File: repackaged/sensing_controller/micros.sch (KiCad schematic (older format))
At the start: 6 parts

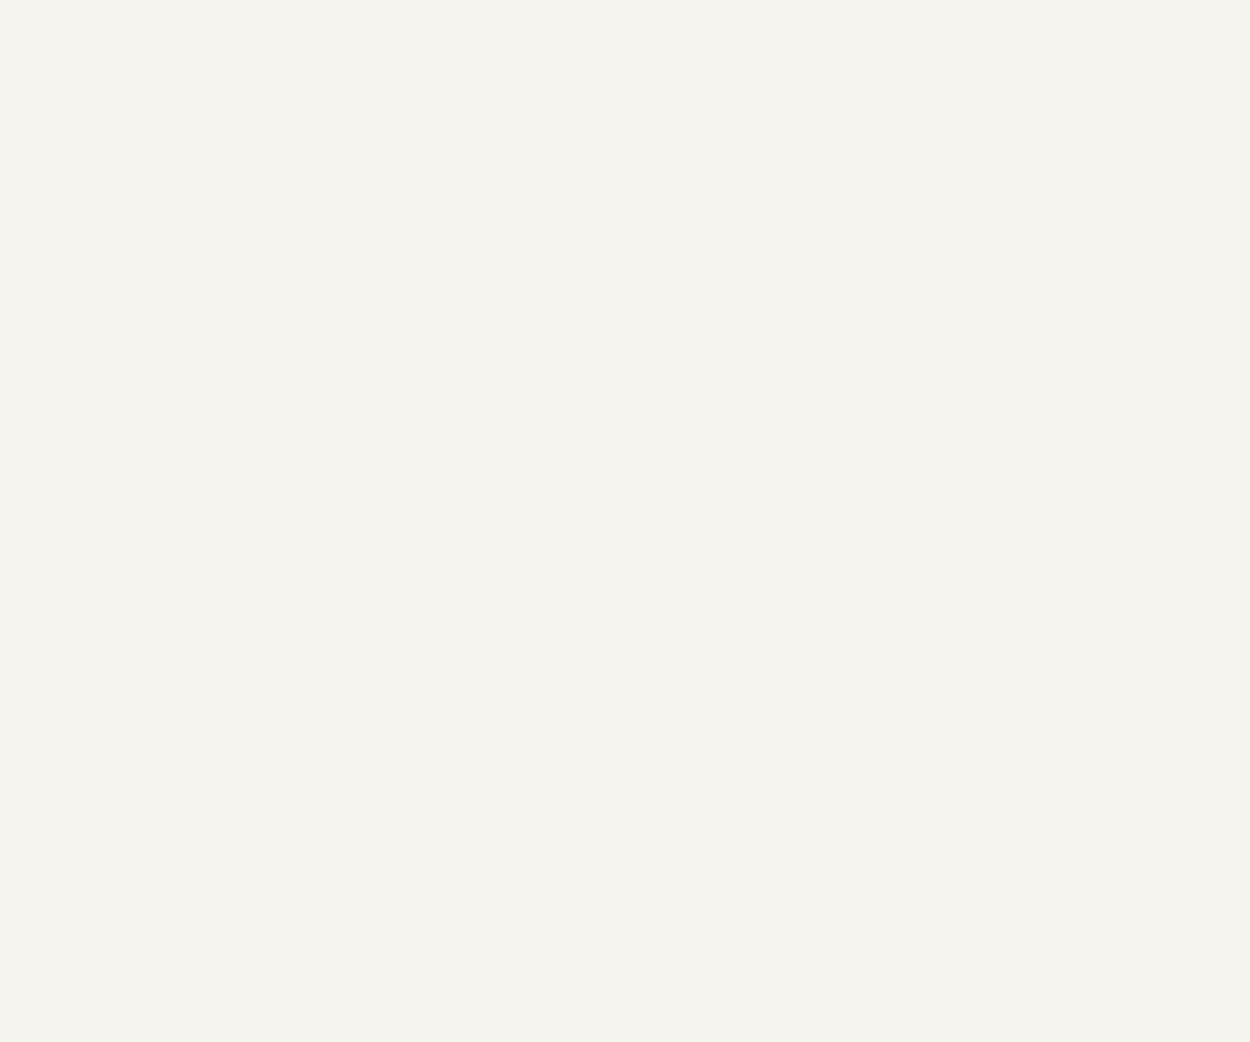
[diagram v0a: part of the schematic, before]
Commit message: Add micro.sch with added components.
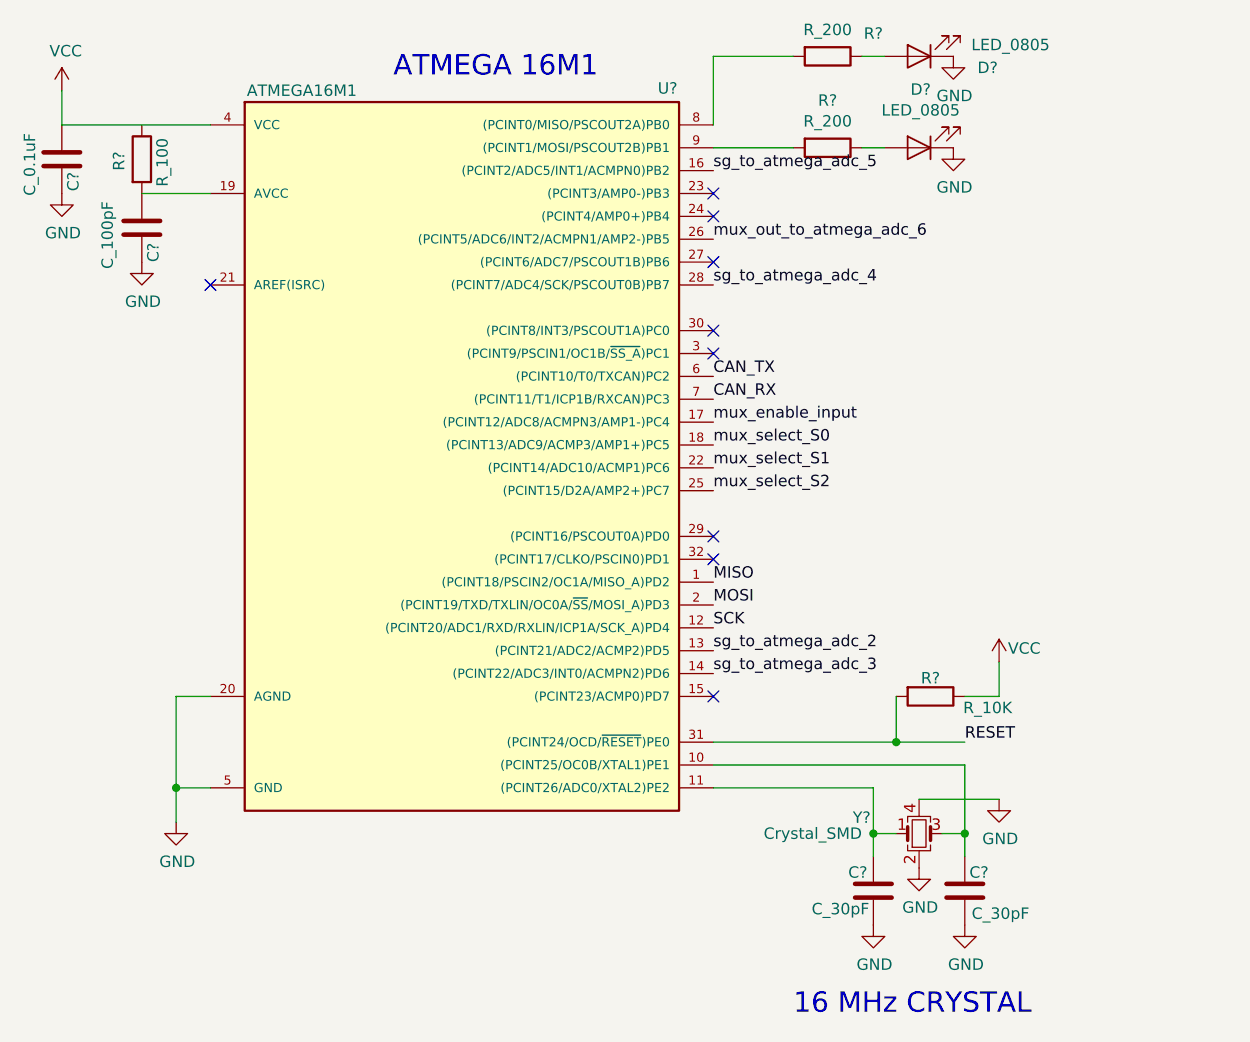
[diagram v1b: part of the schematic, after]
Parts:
- added C?: C_100pF, footprints:C_0805_OEM, symbol formula:C_100pF
- added C? (x2): C_30pF, footprints:C_0805_OEM, symbol formula:C_30pF
- added C?: C_0.1uF, footprints:C_0805_OEM, symbol formula:C_0.1uF
- added D? (x2): LED_0805, footprints:LED_0805_OEM, symbol formula:LED_0805
- added R?: R_100, footprints:R_0805_OEM, symbol formula:R_100
- added R?: R_10K, footprints:R_0805_OEM, symbol formula:R_10K
- added R? (x2): R_200, footprints:R_0805_OEM, symbol formula:R_200
- added U?: ATMEGA16M1, footprints:TQFP-32_7x7mm_Pitch0.8mm, symbol formula:ATMEGA16M1
- added Y?: Crystal_SMD, footprints:Crystal_SMD_FA238, symbol formula:Crystal_SMD
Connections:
- net GND: now also C?.2, C?.2, C?.2, C?.2, D?.1 (K), D?.1 (K), U?.20 (AGND), U?.5 (GND), Y?.2, Y?.4
- new net: C?.1, R?.2, U?.19 (AVCC)
- new net: C?.1, U?.11 ((PCINT26/ADC0/XTAL2)PE2), Y?.1
- new net: C?.1, U?.10 ((PCINT25/OC0B/XTAL1)PE1), Y?.3
- new net: R?.2, U?.8 ((PCINT0/MISO/PSCOUT2A)PB0)
- new net: R?.2, U?.9 ((PCINT1/MOSI/PSCOUT2B)PB1)
- new net: D?.2 (A), R?.1 (x2)
- new net CAN_RX: U?.7 ((PCINT11/T1/ICP1B/RXCAN)PC3)
- new net CAN_TX: U?.6 ((PCINT10/T0/TXCAN)PC2)
- new net MISO: U?.1 ((PCINT18/PSCIN2/OC1A/MISO_A)PD2)
- new net MOSI: U?.2 ((PCINT19/TXD/TXLIN/OC0A/~SS~/MOSI_A)PD3)
- new net RESET: R?.2, U?.31 ((PCINT24/OCD/~RESET~)PE0)
- new net SCK: U?.12 ((PCINT20/ADC1/RXD/RXLIN/ICP1A/SCK_A)PD4)
- new net VCC: C?.1, R?.1, U?.4 (VCC)
- new net mux_enable_input: U?.17 ((PCINT12/ADC8/ACMPN3/AMP1-)PC4)
- new net mux_out_to_atmega_adc_6: U?.26 ((PCINT5/ADC6/INT2/ACMPN1/AMP2-)PB5)
- new net mux_select_S0: U?.18 ((PCINT13/ADC9/ACMP3/AMP1+)PC5)
- new net mux_select_S1: U?.22 ((PCINT14/ADC10/ACMP1)PC6)
- new net mux_select_S2: U?.25 ((PCINT15/D2A/AMP2+)PC7)
- new net sg_to_atmega_adc_2: U?.13 ((PCINT21/ADC2/ACMP2)PD5)
- new net sg_to_atmega_adc_3: U?.14 ((PCINT22/ADC3/INT0/ACMPN2)PD6)
- new net sg_to_atmega_adc_4: U?.28 ((PCINT7/ADC4/SCK/PSCOUT0B)PB7)
- new net sg_to_atmega_adc_5: U?.16 ((PCINT2/ADC5/INT1/ACMPN0)PB2)
- no-connect marks 15 -> 24
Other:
- note added: "ATMEGA 16M1\n"

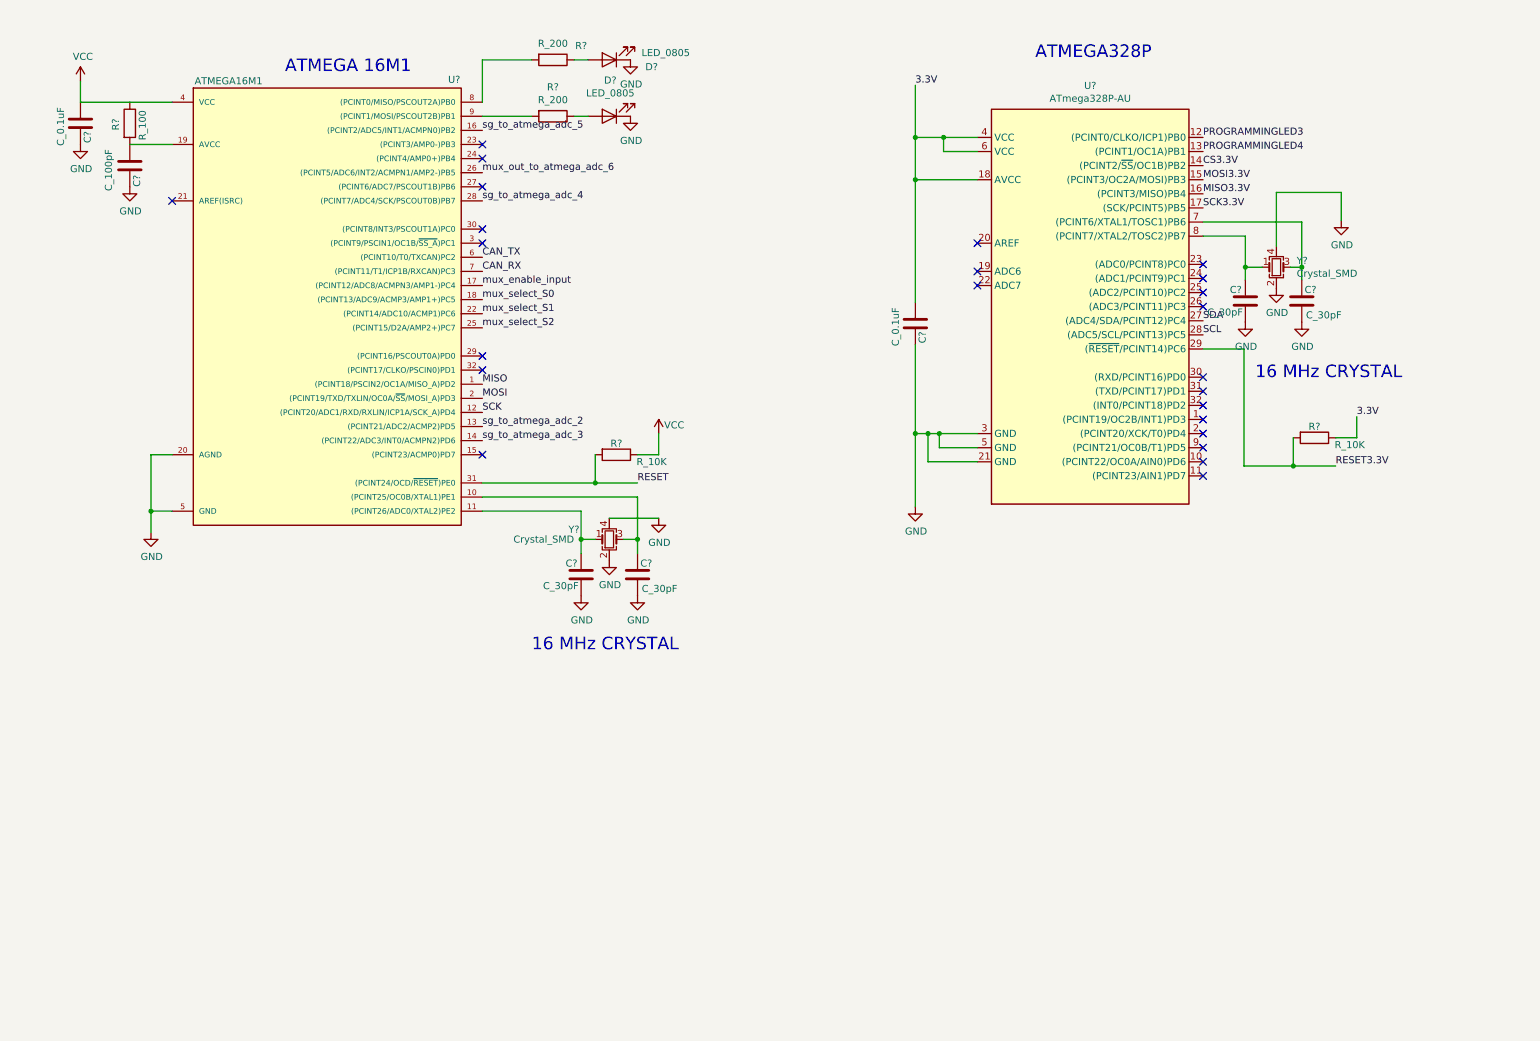
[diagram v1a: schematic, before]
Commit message: Add updated micros.sch
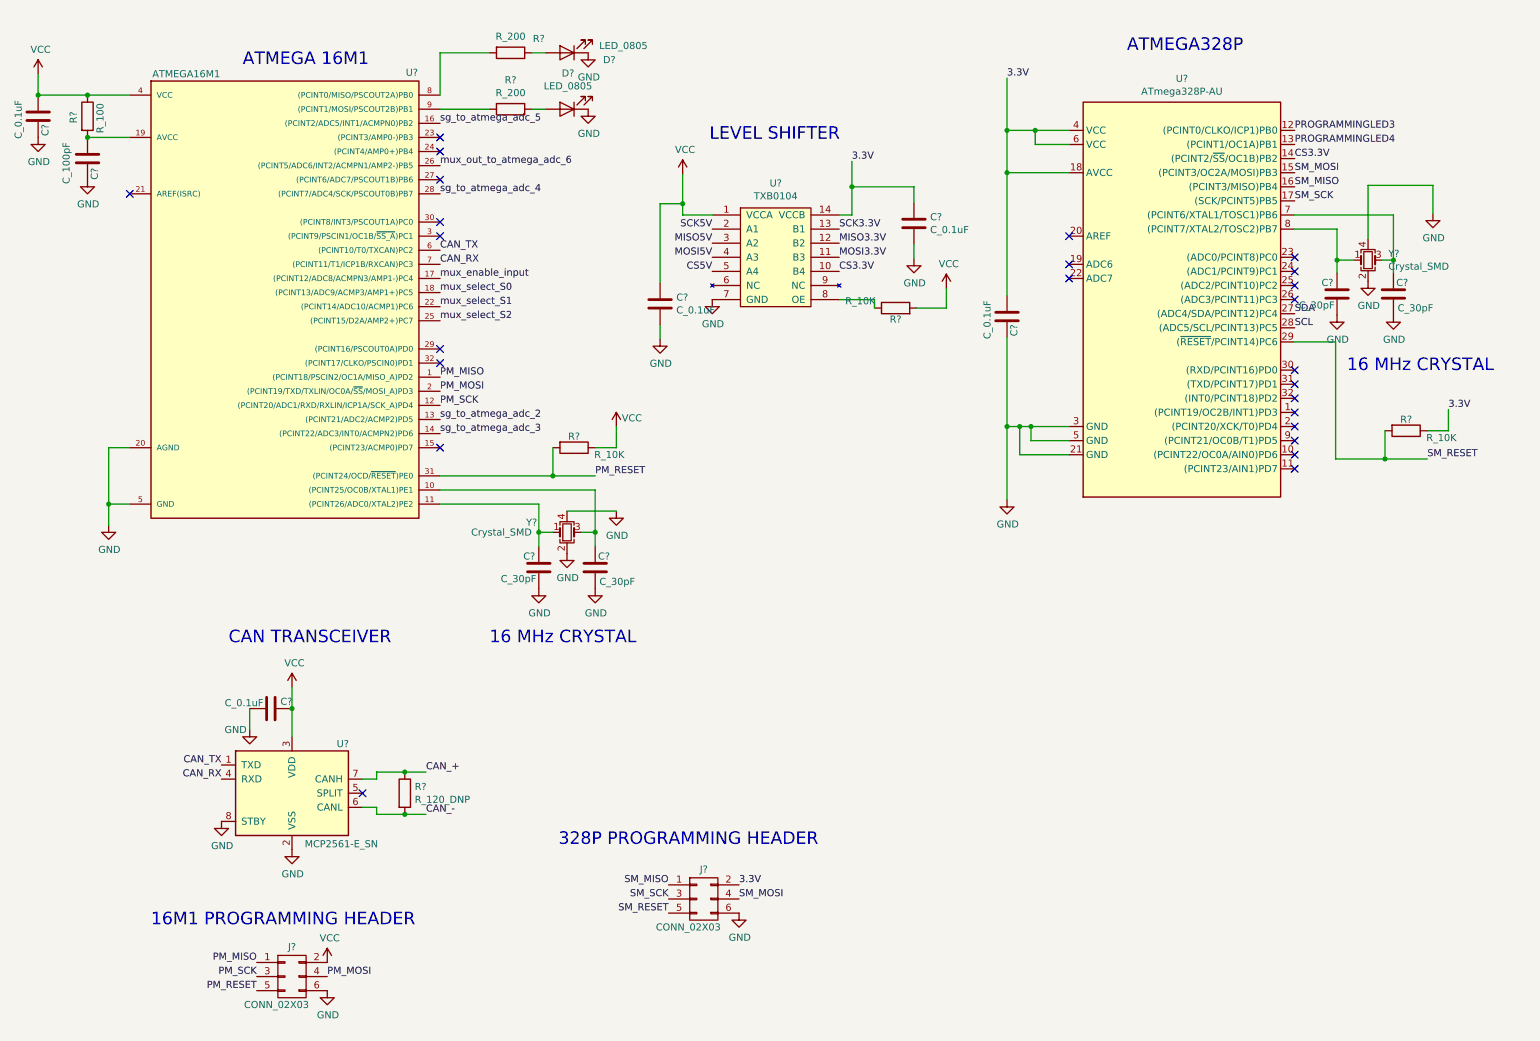
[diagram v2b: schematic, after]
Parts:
- added C? (x3): C_0.1uF, footprints:C_0805_OEM, symbol formula:C_0.1uF
- added J? (x2): CONN_02X03, footprints:Pin_Header_Straight_2x03, symbol formula:CONN_02X03
- added R?: R_120_DNP, footprints:R_0805_OEM, symbol formula:R_120_DNP
- added R?: R_10K, footprints:R_0805_OEM, symbol formula:R_10K
- added U?: MCP2561-E_SN, footprints:SOIC-8_3.9x4.9mm_Pitch1.27mm_OEM, symbol formula:MCP2561-E_SN
- added U?: TXB0104, Housings_SSOP:TSSOP-14_4.4x5mm_Pitch0.65mm, symbol formula:TXB0104
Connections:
- net 3.3V: now also C?.1, J?.2 (P2), U?.14 (VCCB)
- net CAN_RX: now also U?.4 (RXD)
- net CAN_TX: now also U?.1 (TXD)
- net CS3.3V: now also U?.10 (B4)
- net GND: now also C?.2, C?.2, C?.2, J?.6 (P6), J?.6 (P6), U?.2 (VSS), U?.7 (GND), U?.8 (STBY)
- net MISO3.3V: now also U?.12 (B2); no longer U?.16 ((PCINT3/MISO)PB4)
- net MOSI3.3V: now also U?.11 (B3); no longer U?.15 ((PCINT3/OC2A/MOSI)PB3)
- net SCK3.3V: now also U?.13 (B1); no longer U?.17 ((SCK/PCINT5)PB5)
- net VCC: now also R?.1, C?.1, C?.1, J?.2 (P2), R?.2, U?.1 (VCCA), U?.3 (VDD)
- net MISO renamed PM_MISO
- net PM_MISO: now also J?.1 (P1)
- net MOSI renamed PM_MOSI
- net PM_MOSI: now also J?.4 (P4)
- net RESET renamed PM_RESET
- net PM_RESET: now also J?.5 (P5)
- net RESET3.3V renamed SM_RESET
- net SM_RESET: now also J?.5 (P5)
- net SCK renamed PM_SCK
- net PM_SCK: now also J?.3 (P3)
- new net: R?.1, U?.8 (OE)
- new net CAN_+: R?.1, U?.7 (CANH)
- new net CAN_-: R?.2, U?.6 (CANL)
- new net CS5V: U?.5 (A4)
- new net MISO5V: U?.3 (A2)
- new net MOSI5V: U?.4 (A3)
- new net SCK5V: U?.2 (A1)
- new net SM_MISO: J?.1 (P1), U?.16 ((PCINT3/MISO)PB4)
- new net SM_MOSI: J?.4 (P4), U?.15 ((PCINT3/OC2A/MOSI)PB3)
- new net SM_SCK: J?.3 (P3), U?.17 ((SCK/PCINT5)PB5)
- no-connect marks 24 -> 25
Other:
- note added: "16M1 PROGRAMMING HEADER\n"
- note added: "328P PROGRAMMING HEADER\n"
- note added: "CAN TRANSCEIVER\n"
- note added: "LEVEL SHIFTER"
- moved on the sheet: C?, D?, R?, U?, Y?
